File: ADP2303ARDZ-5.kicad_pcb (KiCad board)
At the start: 2 copper layers, 11 parts, among them P1 CONN_01X05, P2 CONN_01X03, U1 ADP2303ARDZ

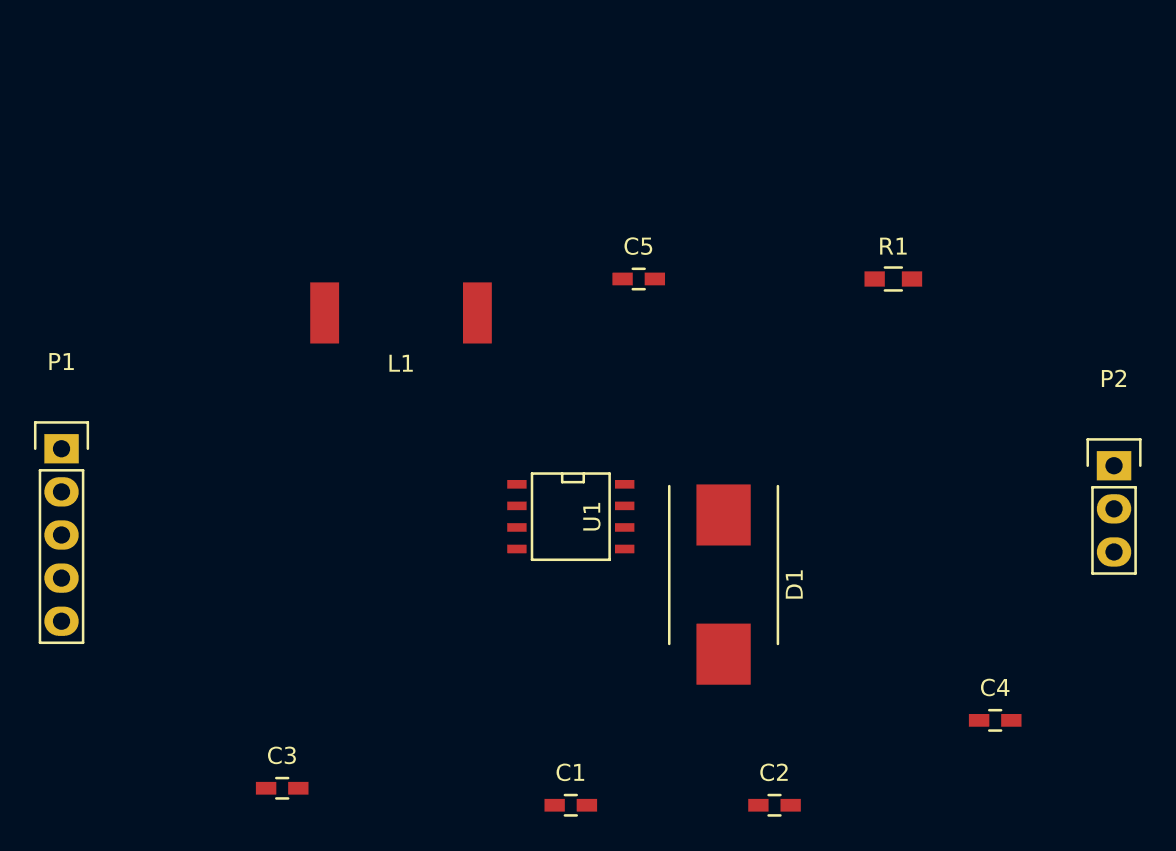
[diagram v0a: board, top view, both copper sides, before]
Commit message: moved to v5 footprints so a few missing
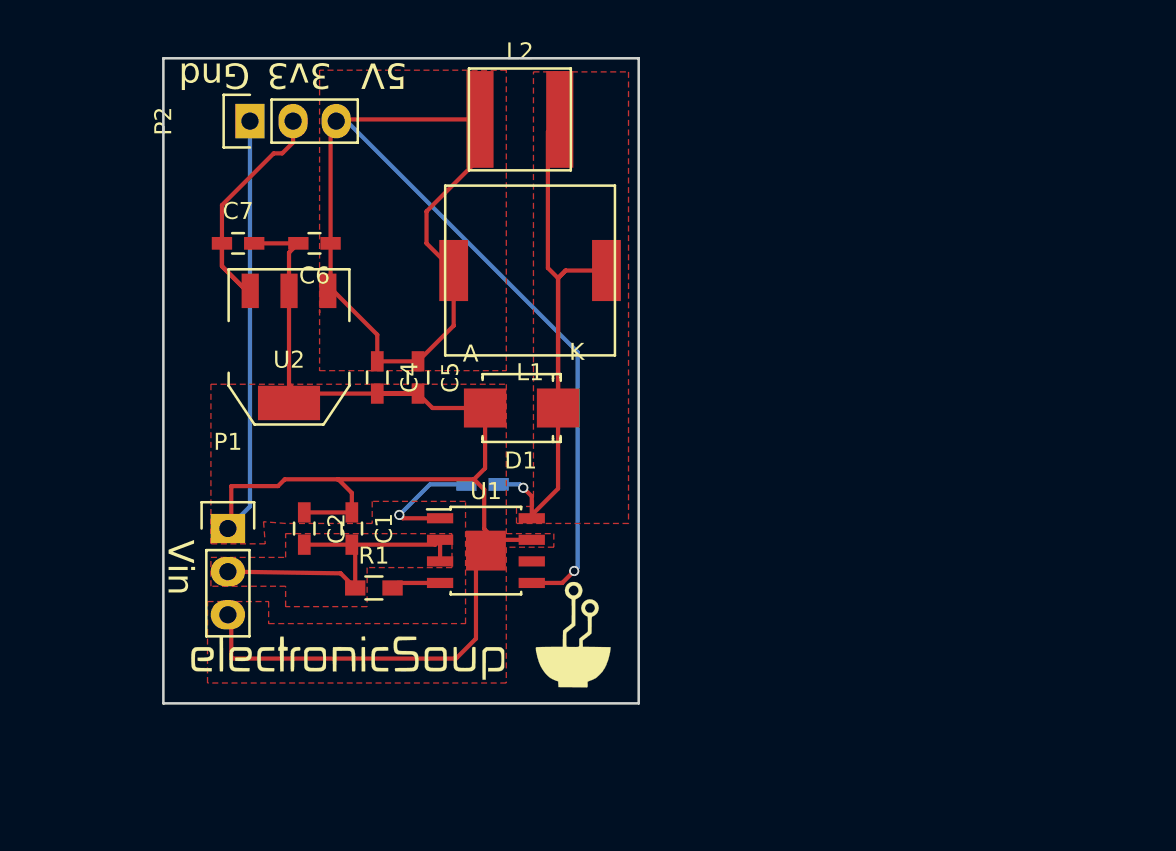
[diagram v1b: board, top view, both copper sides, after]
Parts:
- added C6: 0.1uF, Capacitors_SMD:C_0603_HandSoldering, F.Cu at (132.9, 90.9)
- added C7: 0.1uF, Capacitors_SMD:C_0603_HandSoldering, F.Cu at (128.4, 90.9)
- added G***: LOGO, electronicSoup:LOGO, F.Cu at (139.0, 114.0)
- added L2: 3uH, electronicSoup:Inductor-SRN6028-Series, F.Cu at (145.0, 83.6)
- added U2: MCP1825S, TO_SOT_Packages_SMD:SOT-223, F.Cu at (131.4, 97.0)
- C3: moved to B.Cu
- D1: footprint Diodes_SMD:DO-214AB_Handsoldering -> Diodes_SMD:SMB_Standard
- L1: value VLF10040T-4R7N5R4 -> 4.7uH; footprint electronicSoup:VLF10040_Inductor -> electronicSoup:Inductor-VLF10040
- P1: value CONN_01X05 -> CONN_01X03; footprint Pin_Headers:Pin_Header_Straight_1x05 -> Pin_Headers:Pin_Header_Straight_1x03
- U1: value ADP2303ARDZ -> ADP230x; footprint SMD_Packages:SOIC-8-N -> Housings_SOIC:SOIC-8-1EP_3.9x4.9mm_Pitch1.27mm
- moved P2 54.8 mm to (129.1, 83.7), turned to 90 degrees
- moved C4 41.6 mm to (136.6, 98.8), turned to 270 degrees
- moved R1 35.6 mm to (136.4, 111.2)
- moved C2 32.1 mm to (132.3, 107.7), turned to 270 degrees
- moved C3 21.4 mm to (142.8, 105.1)
- moved C1 20.8 mm to (135.1, 107.7), turned to 270 degrees
- moved D1 15.8 mm to (145.1, 100.6), turned to 180 degrees
- moved C5 14.2 mm to (139.0, 98.8), turned to 270 degrees
- moved P1 10.9 mm to (127.8, 107.7)
- moved L1 8.00 mm to (145.6, 92.5)
- moved U1 5.39 mm to (143.0, 109.0), turned to 0 degrees
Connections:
- net Net-(C3-Pad1) renamed /BST
- net Net-(C3-Pad2) renamed /SW
- C4 pad 1: /Vout -> /5V
- C5 pad 1: /Vout -> /5V
- L1 pad 2: /Vout -> /5V
- P1 pad 2: /Gnd -> /Vin
- P1 pad 3: /Vin -> /Gnd
- P2 pad 1: /Vout -> /Gnd
- P2 pad 2: Net-(P2-Pad2) -> /3v3
- P2 pad 3: /Gnd -> /5V
- U1 pad 5: /Vout -> /5V
- U1 pad 6: Net-(U1-Pad6) -> (no net)
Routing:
- net /Gnd: track 0.00 -> 110.8 mm
- net /5V: track 0.00 -> 79.1 mm, vias 0 -> 1
- net /SW: track 0.00 -> 38.5 mm, vias 0 -> 1
- net /Vin: track 0.00 -> 19.9 mm
- net /3v3: track 0.00 -> 16.2 mm
- net /BST: track 0.00 -> 7.18 mm, vias 0 -> 1
- net Net-(R1-Pad2): track 0.00 -> 2.92 mm
- added copper zone on F.Cu, net /5V
- added copper zone on B.Cu, net /Gnd
- added copper zone on F.Cu, net /Gnd
- added copper zone on F.Cu, net /SW
- added copper zone on F.Cu, net /Vin
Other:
- board outline added: 28 x 38 mm
- board text added: "3v3"
- board text added: "5V"
- board text added: "Gnd"
- board text added: "Vin"
